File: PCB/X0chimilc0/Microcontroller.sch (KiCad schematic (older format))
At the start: 2 parts

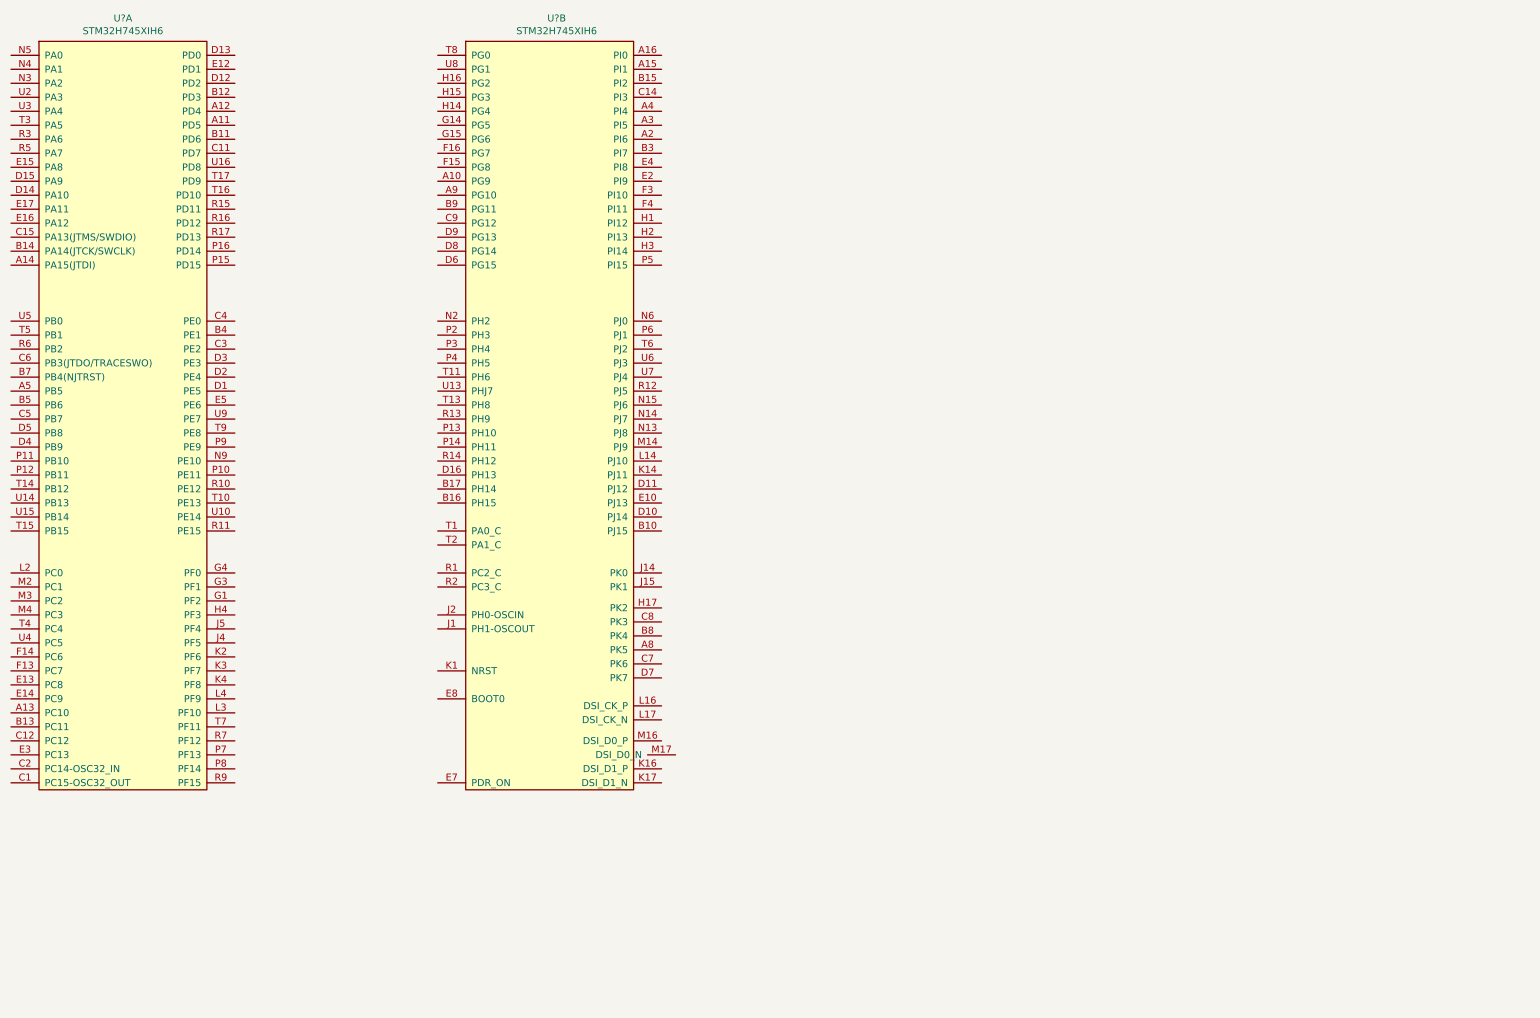
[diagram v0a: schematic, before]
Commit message: PCB Mockup
Made components for DAC/MCU/FPGA/Connectors, mocked things up as PCB, going to be crazy.
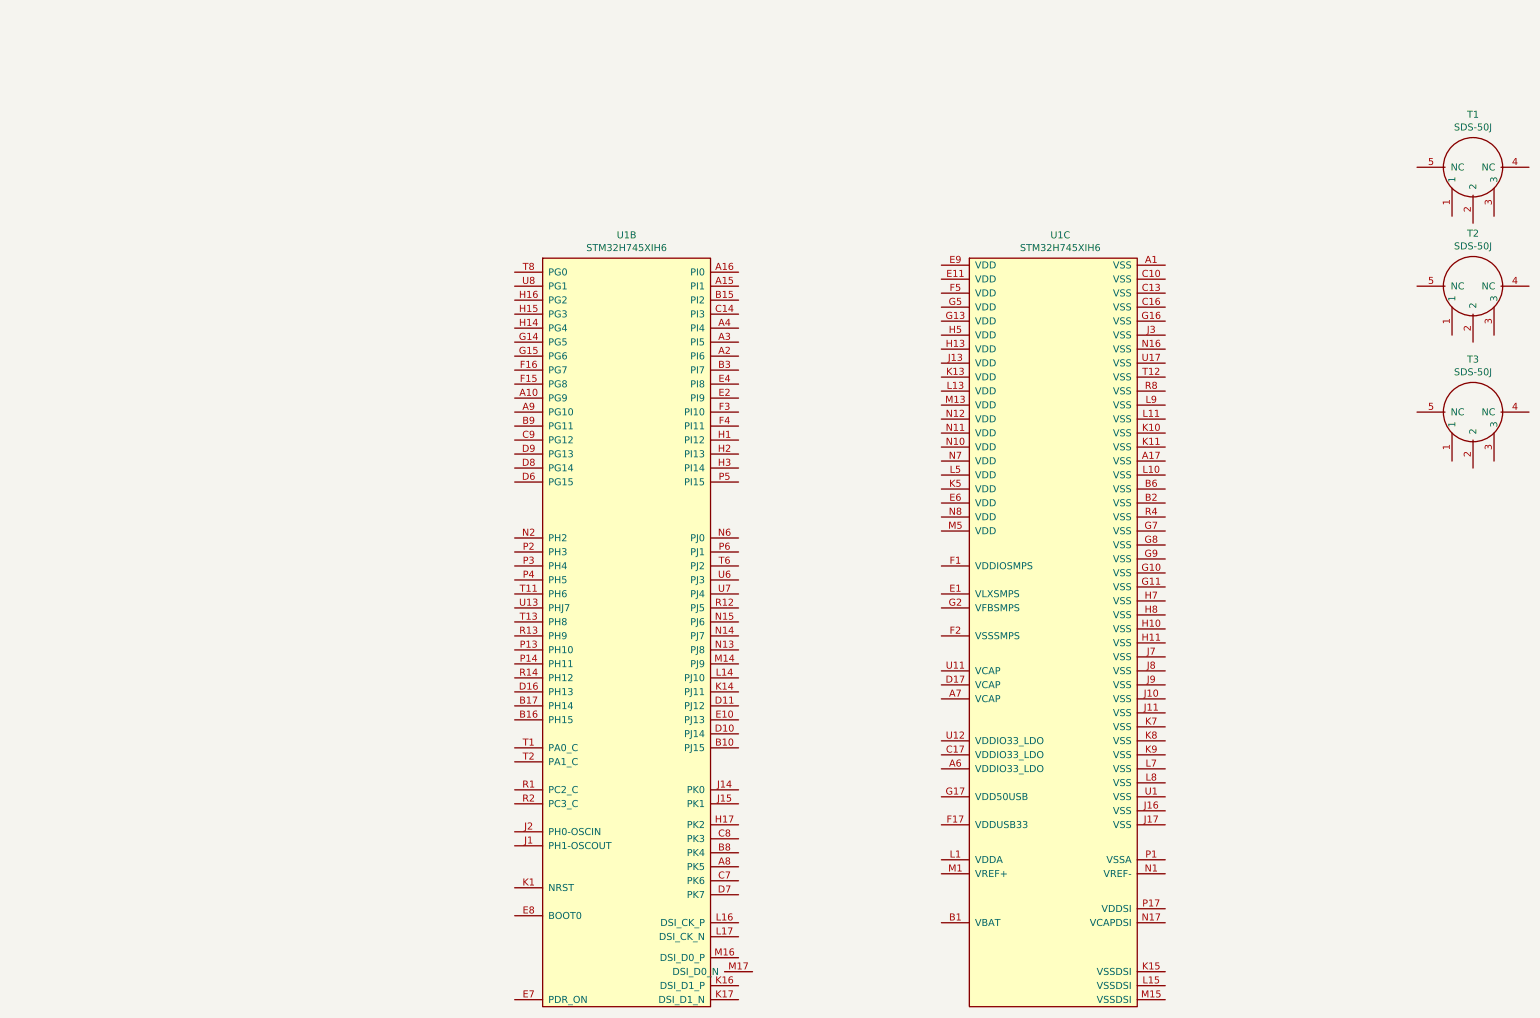
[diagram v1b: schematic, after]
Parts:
- added T1, T2, T3: SDS-50J, AVR-KiCAD-Lib-ICs:SDS-50J, symbol AVR-KiCAD-Lib-Connectors:SDS-50J
- gave numbers to parts that had none: 1

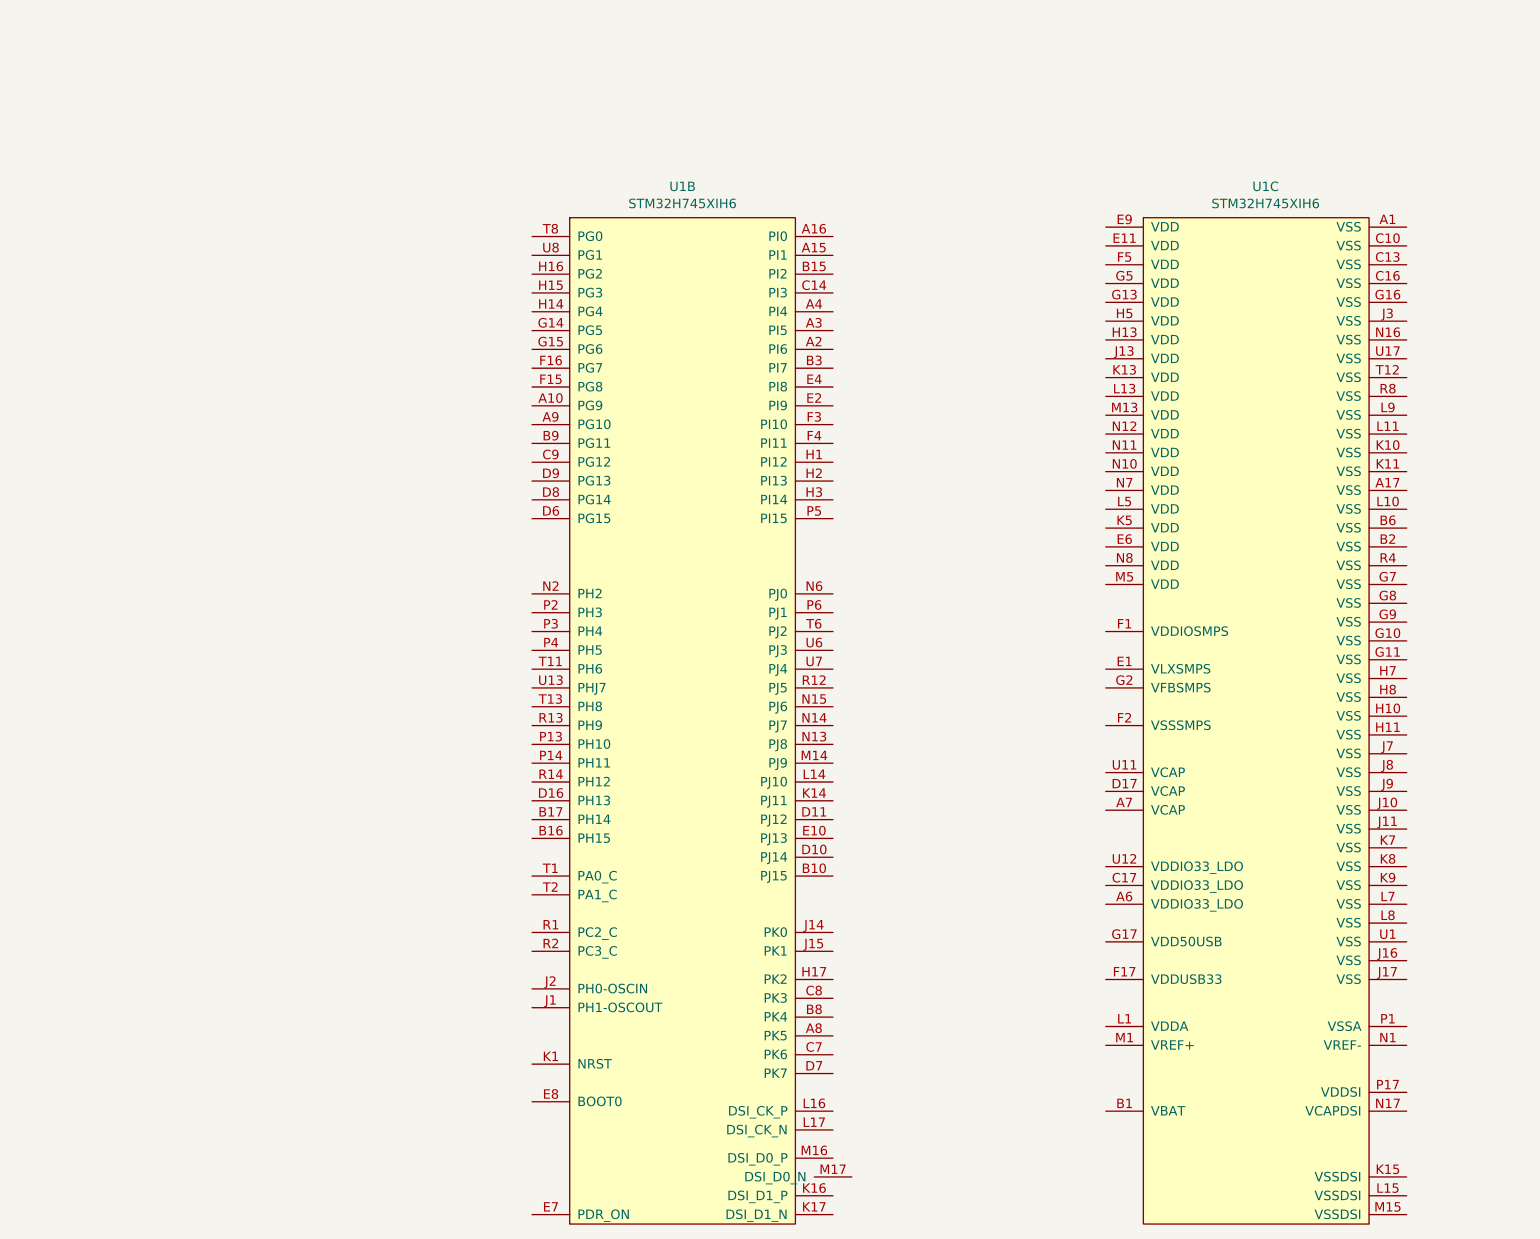
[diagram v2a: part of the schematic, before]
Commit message: Component PDFs
added relevant PDF datasheets and some minor schematic edits
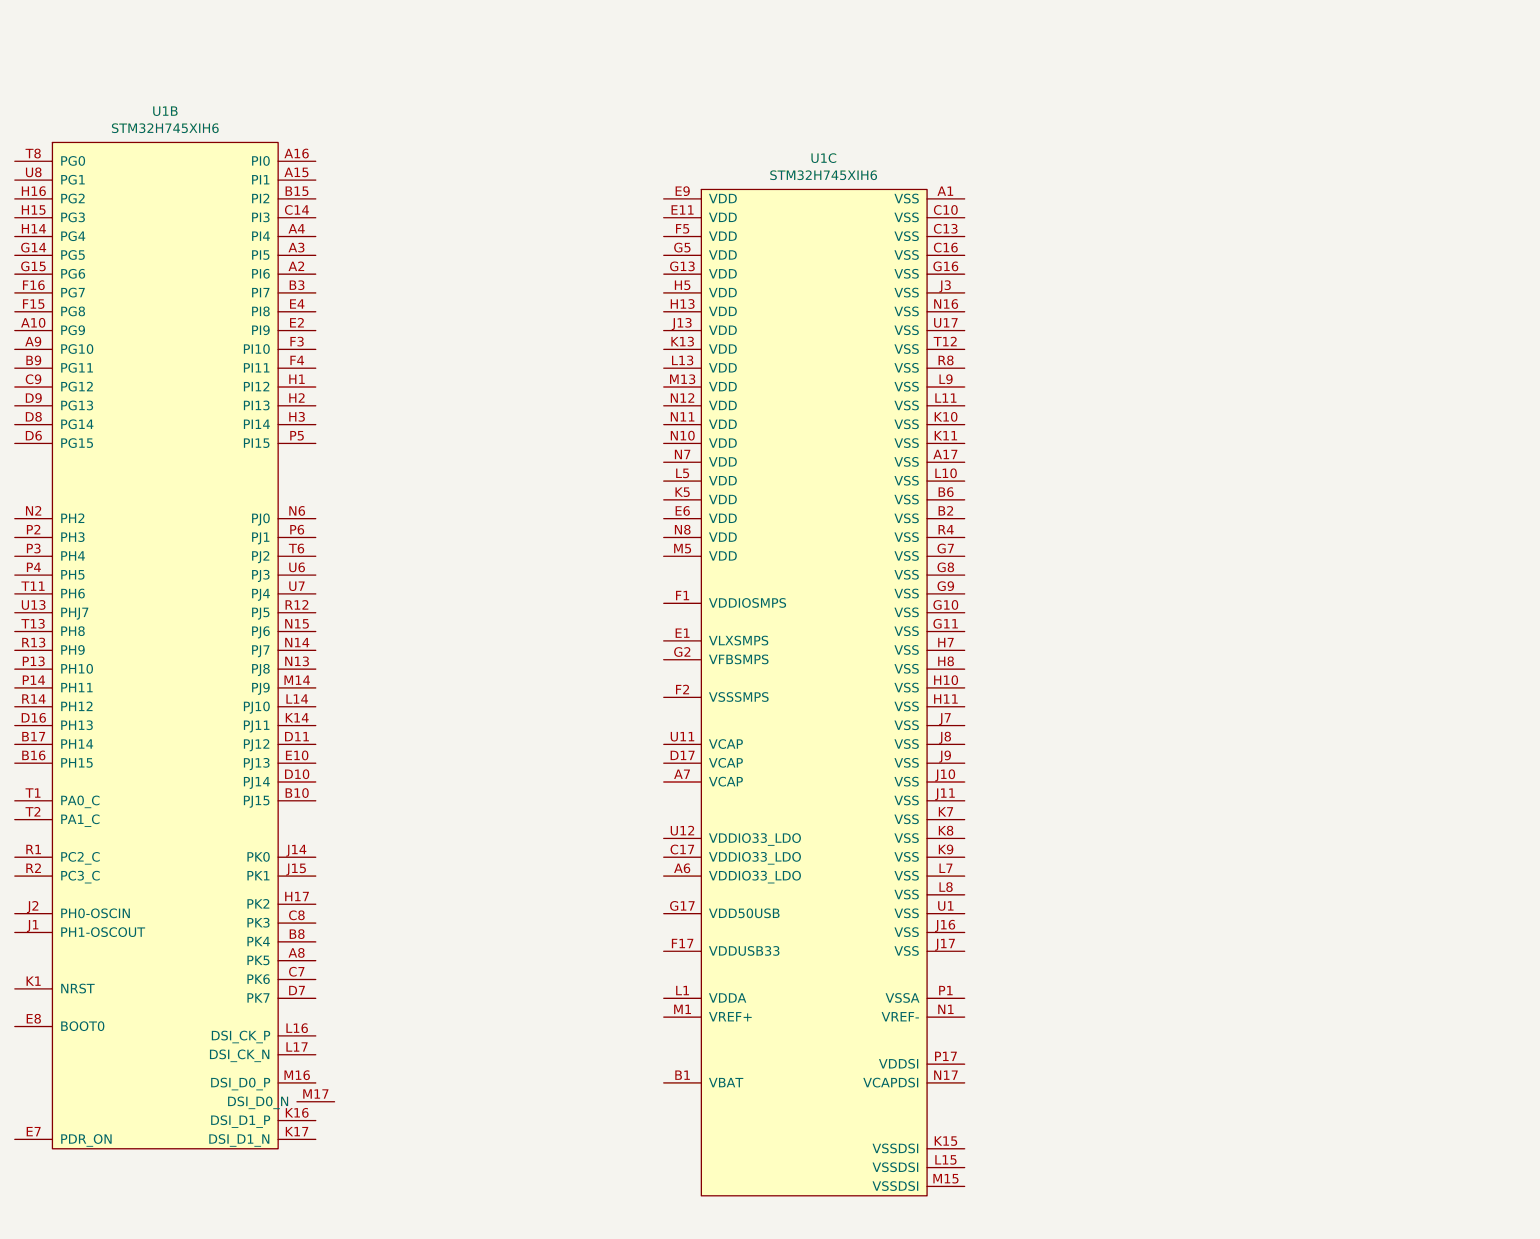
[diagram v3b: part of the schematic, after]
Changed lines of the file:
@@
 $EndDescr
-$Comp
-L AVR-KiCAD-Lib-ICs:STM32H745XIH6 U1
-U 2 1 5E2E3E4B
-P 6550 2500
-F 0 "U1" H 6150 2665 50  0000 C CNN
-F 1 "STM32H745XIH6" H 6600 2700 50  0001 C CNN
-F 2 "AVR-KiCAD-Lib-ICs:STM32H745XIH6" H 6350 2500 50  0001 C CNN
-F 3 "https://www.st.com/resource/en/datasheet/stm32h745ii.pdf" H 6450 2600 50  0001 C CNN
-F 4 "17.02000" H 6650 2750 50  0001 C CNN "Cost QTY: 1"
-F 5 "11.75168" H 6750 2850 50  0001 C CNN "Cost QTY: 1000"
-F 6 "11.75168" H 6850 2950 50  0001 C CNN "Cost QTY: 2500"
-F 7 "11.75168" H 6950 3050 50  0001 C CNN "Cost QTY: 5000"
-F 8 "11.75168" H 7050 3150 50  0001 C CNN "Cost QTY: 10000"
-F 9 "STMicroelectronics" H 7150 3250 50  0001 C CNN "MFR"
-F 10 "STM32H745XIH6" H 7250 3350 50  0001 C CNN "MFR#"
-F 11 "Digikey" H 7350 3450 50  0001 C CNN "Vendor"
-F 12 "497-19502-ND" H 7450 3550 50  0001 C CNN "Vendor #"
-F 13 "AVR" H 7550 3650 50  0001 C CNN "Designer"
-F 14 "0.76mm" H 7650 3750 50  0001 C CNN "Height"
-F 15 "11/29/2019" H 8750 4850 50  0001 C CNN "Date Created"
-F 16 "11/29/2019" H 7750 3850 50  0001 C CNN "Date Modified"
-F 17 "Yes" H 7850 3950 50  0001 C CNN "Lead-Free ?"
-F 18 "1" H 7950 4050 50  0001 C CNN "RoHS Levels"
-F 19 "SMT" H 8050 4150 50  0001 C CNN "Mounting"
-F 20 "265" H 8150 4250 50  0001 C CNN "Pin Count #"
-F 21 "Active" H 8250 4350 50  0001 C CNN "Status"
-F 22 "*" H 8350 4450 50  0001 C CNN "Tolerance"
-F 23 "Microcontroller Dual Core" H 8450 4550 50  0001 C CNN "Type"
-F 24 "3.3V" H 8550 4650 50  0001 C CNN "Voltage"
-F 25 "BGA" H 8650 4800 50  0001 C CNN "Package"
-F 26 "ARM® Cortex®-M4, Cortex®-M7 STM32H7 Microcontroller IC 32-Bit Dual-Core 240MHz, 480MHz 2MB (2M x 8) FLASH 240+25-TFBGA (14x14)" H 8950 5100 50  0001 C CNN "Description"
-F 27 "STM32H745XIH6" H 6150 2574 50  0000 C CNN "_Value_"
-F 28 "*" H 8950 5100 50  0001 C CNN "Management_ID"
-	2    6550 2500
-	1    0    0    -1
-$EndComp
-$Comp
-L AVR-KiCAD-Lib-ICs:STM32H745XIH6 U1
-U 3 1 5E2F607C
-P 9600 2500
-F 0 "U1" H 9250 2665 50  0000 C CNN
-F 1 "STM32H745XIH6" H 9650 2700 50  0001 C CNN
-F 2 "AVR-KiCAD-Lib-ICs:STM32H745XIH6" H 9400 2500 50  0001 C CNN
-F 3 "https://www.st.com/resource/en/datasheet/stm32h745ii.pdf" H 9500 2600 50  0001 C CNN
-F 4 "17.02000" H 9700 2750 50  0001 C CNN "Cost QTY: 1"
-F 5 "11.75168" H 9800 2850 50  0001 C CNN "Cost QTY: 1000"
-F 6 "11.75168" H 9900 2950 50  0001 C CNN "Cost QTY: 2500"
-F 7 "11.75168" H 10000 3050 50  0001 C CNN "Cost QTY: 5000"
-F 8 "11.75168" H 10100 3150 50  0001 C CNN "Cost QTY: 10000"
-F 9 "STMicroelectronics" H 10200 3250 50  0001 C CNN "MFR"
-F 10 "STM32H745XIH6" H 10300 3350 50  0001 C CNN "MFR#"
-F 11 "Digikey" H 10400 3450 50  0001 C CNN "Vendor"
-F 12 "497-19502-ND" H 10500 3550 50  0001 C CNN "Vendor #"
-F 13 "AVR" H 10600 3650 50  0001 C CNN "Designer"
-F 14 "0.76mm" H 10700 3750 50  0001 C CNN "Height"
-F 15 "11/29/2019" H 11800 4850 50  0001 C CNN "Date Created"
-F 16 "11/29/2019" H 10800 3850 50  0001 C CNN "Date Modified"
-F 17 "Yes" H 10900 3950 50  0001 C CNN "Lead-Free ?"
-F 18 "1" H 11000 4050 50  0001 C CNN "RoHS Levels"
-F 19 "SMT" H 11100 4150 50  0001 C CNN "Mounting"
-F 20 "265" H 11200 4250 50  0001 C CNN "Pin Count #"
-F 21 "Active" H 11300 4350 50  0001 C CNN "Status"
-F 22 "*" H 11400 4450 50  0001 C CNN "Tolerance"
-F 23 "Microcontroller Dual Core" H 11500 4550 50  0001 C CNN "Type"
-F 24 "3.3V" H 11600 4650 50  0001 C CNN "Voltage"
-F 25 "BGA" H 11700 4800 50  0001 C CNN "Package"
-F 26 "ARM® Cortex®-M4, Cortex®-M7 STM32H7 Microcontroller IC 32-Bit Dual-Core 240MHz, 480MHz 2MB (2M x 8) FLASH 240+25-TFBGA (14x14)" H 12000 5100 50  0001 C CNN "Description"
-F 27 "STM32H745XIH6" H 9250 2574 50  0000 C CNN "_Value_"
-F 28 "*" H 12000 5100 50  0001 C CNN "Management_ID"
-	3    9600 2500
-	1    0    0    -1
-$EndComp
 $Comp
 L AVR-KiCAD-Lib-Connectors:SDS-50J T1
@@
 	1    0    0    -1
 $EndComp
+$Comp
+L AVR-KiCAD-Lib-ICs:STM32H745XIH6 U1
+U 2 1 5DEF1B05
+P 3800 2100
+F 0 "U1" H 3400 2265 50  0000 C CNN
+F 1 "STM32H745XIH6" H 3850 2300 50  0001 C CNN
+F 2 "AVR-KiCAD-Lib-ICs:STM32H745XIH6" H 3600 2100 50  0001 C CNN
+F 3 "https://www.st.com/resource/en/datasheet/stm32h745ii.pdf" H 3700 2200 50  0001 C CNN
+F 4 "17.02000" H 3900 2350 50  0001 C CNN "Cost QTY: 1"
+F 5 "11.75168" H 4000 2450 50  0001 C CNN "Cost QTY: 1000"
+F 6 "11.75168" H 4100 2550 50  0001 C CNN "Cost QTY: 2500"
+F 7 "11.75168" H 4200 2650 50  0001 C CNN "Cost QTY: 5000"
+F 8 "11.75168" H 4300 2750 50  0001 C CNN "Cost QTY: 10000"
+F 9 "STMicroelectronics" H 4400 2850 50  0001 C CNN "MFR"
+F 10 "STM32H745XIH6" H 4500 2950 50  0001 C CNN "MFR#"
+F 11 "Digikey" H 4600 3050 50  0001 C CNN "Vendor"
+F 12 "497-19502-ND" H 4700 3150 50  0001 C CNN "Vendor #"
+F 13 "AVR" H 4800 3250 50  0001 C CNN "Designer"
+F 14 "0.76mm" H 4900 3350 50  0001 C CNN "Height"
+F 15 "11/29/2019" H 6000 4450 50  0001 C CNN "Date Created"
+F 16 "11/29/2019" H 5000 3450 50  0001 C CNN "Date Modified"
+F 17 "Yes" H 5100 3550 50  0001 C CNN "Lead-Free ?"
+F 18 "1" H 5200 3650 50  0001 C CNN "RoHS Levels"
+F 19 "SMT" H 5300 3750 50  0001 C CNN "Mounting"
+F 20 "265" H 5400 3850 50  0001 C CNN "Pin Count #"
+F 21 "Active" H 5500 3950 50  0001 C CNN "Status"
+F 22 "*" H 5600 4050 50  0001 C CNN "Tolerance"
+F 23 "Microcontroller Dual Core" H 5700 4150 50  0001 C CNN "Type"
+F 24 "3.3V" H 5800 4250 50  0001 C CNN "Voltage"
+F 25 "BGA" H 5900 4400 50  0001 C CNN "Package"
+F 26 "ARM® Cortex®-M4, Cortex®-M7 STM32H7 Microcontroller IC 32-Bit Dual-Core 240MHz, 480MHz 2MB (2M x 8) FLASH 240+25-TFBGA (14x14)" H 6200 4700 50  0001 C CNN "Description"
+F 27 "STM32H745XIH6" H 3400 2174 50  0000 C CNN "_Value_"
+F 28 "*" H 6200 4700 50  0001 C CNN "Management_ID"
+	2    3800 2100
+	1    0    0    -1
+$EndComp
+$Comp
+L AVR-KiCAD-Lib-ICs:STM32H745XIH6 U1
+U 3 1 5DEF6B96
+P 7250 2350
+F 0 "U1" H 6900 2515 50  0000 C CNN
+F 1 "STM32H745XIH6" H 7300 2550 50  0001 C CNN
+F 2 "AVR-KiCAD-Lib-ICs:STM32H745XIH6" H 7050 2350 50  0001 C CNN
+F 3 "https://www.st.com/resource/en/datasheet/stm32h745ii.pdf" H 7150 2450 50  0001 C CNN
+F 4 "17.02000" H 7350 2600 50  0001 C CNN "Cost QTY: 1"
+F 5 "11.75168" H 7450 2700 50  0001 C CNN "Cost QTY: 1000"
+F 6 "11.75168" H 7550 2800 50  0001 C CNN "Cost QTY: 2500"
+F 7 "11.75168" H 7650 2900 50  0001 C CNN "Cost QTY: 5000"
+F 8 "11.75168" H 7750 3000 50  0001 C CNN "Cost QTY: 10000"
+F 9 "STMicroelectronics" H 7850 3100 50  0001 C CNN "MFR"
+F 10 "STM32H745XIH6" H 7950 3200 50  0001 C CNN "MFR#"
+F 11 "Digikey" H 8050 3300 50  0001 C CNN "Vendor"
+F 12 "497-19502-ND" H 8150 3400 50  0001 C CNN "Vendor #"
+F 13 "AVR" H 8250 3500 50  0001 C CNN "Designer"
+F 14 "0.76mm" H 8350 3600 50  0001 C CNN "Height"
+F 15 "11/29/2019" H 9450 4700 50  0001 C CNN "Date Created"
+F 16 "11/29/2019" H 8450 3700 50  0001 C CNN "Date Modified"
+F 17 "Yes" H 8550 3800 50  0001 C CNN "Lead-Free ?"
+F 18 "1" H 8650 3900 50  0001 C CNN "RoHS Levels"
+F 19 "SMT" H 8750 4000 50  0001 C CNN "Mounting"
+F 20 "265" H 8850 4100 50  0001 C CNN "Pin Count #"
+F 21 "Active" H 8950 4200 50  0001 C CNN "Status"
+F 22 "*" H 9050 4300 50  0001 C CNN "Tolerance"
+F 23 "Microcontroller Dual Core" H 9150 4400 50  0001 C CNN "Type"
+F 24 "3.3V" H 9250 4500 50  0001 C CNN "Voltage"
+F 25 "BGA" H 9350 4650 50  0001 C CNN "Package"
+F 26 "ARM® Cortex®-M4, Cortex®-M7 STM32H7 Microcontroller IC 32-Bit Dual-Core 240MHz, 480MHz 2MB (2M x 8) FLASH 240+25-TFBGA (14x14)" H 9650 4950 50  0001 C CNN "Description"
+F 27 "STM32H745XIH6" H 6900 2424 50  0000 C CNN "_Value_"
+F 28 "*" H 9650 4950 50  0001 C CNN "Management_ID"
+	3    7250 2350
+	1    0    0    -1
+$EndComp
